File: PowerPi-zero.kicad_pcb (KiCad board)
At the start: 2 copper layers, 65 x 30 mm, 38 parts, among them J1 2444, J2 JST XH 01x02, J6 Raspberry_Pi_2_3, J8 JST XH 01x02, Q1 30V 4A 44mΩ, Q2 50nA 150V 200mW 200mA, Q3 30V 4A 44mΩ, U1 XL4015

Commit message: Final tweaks for producion
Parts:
- moved F1 1.08 mm to (101.5, 117.1)
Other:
- board text added: "V2.0"
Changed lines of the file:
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@@
     (pad_to_mask_clearance 0)
     (pcbplotparams
-      (layerselection 0x0001330_80000001)
+      (layerselection 0x00013f2_ffffffff)
       (disableapertmacros false)
       (usegerberextensions false)
@@
       (sketchpadsonfab false)
       (subtractmaskfromsilk false)
-      (outputformat 4)
+      (outputformat 1)
       (mirror false)
-      (drillshape 2)
+      (drillshape 0)
       (scaleselection 1)
       (outputdirectory "meta/")
@@
   )
   (footprint "Fuse:Fuse_Littelfuse-NANO2-451_453" (layer "F.Cu")
-    (at 101.5 116 90)
+    (at 101.5 117.085 90)
     (descr "Littelfuse NANO2 https://www.littelfuse.com/~/media/electronics/datasheets/fuses/littelfuse_fuse_451_453_datasheet.pdf.pdf")
     (tags "Fuse Nano2")
@@
     (property "abv.Footprint" "SMD-2_5.03x9.73x3.81")
     (attr smd)
-    (fp_text reference "F1" (at -5 0 90 unlocked) (layer "F.SilkS")
+    (fp_text reference "F1" (at 0 0 90 unlocked) (layer "F.SilkS")
       (effects (font (size 1 1) (thickness 0.15)))
     )
@@
       (effects (font (size 1 1) (thickness 0.15)))
     )
-    (fp_line (start -1.215 1.455) (end 1.215 1.455) (layer "F.SilkS") (width 0.12))
-    (fp_line (start -1.215 -1.455) (end 1.215 -1.455) (layer "F.SilkS") (width 0.12))
-    (fp_line (start -3.69 -1.83) (end 3.69 -1.83) (layer "F.CrtYd") (width 0.05))
-    (fp_line (start 3.69 -1.83) (end 3.69 1.83) (layer "F.CrtYd") (width 0.05))
-    (fp_line (start -3.69 1.83) (end -3.69 -1.83) (layer "F.CrtYd") (width 0.05))
-    (fp_line (start 3.69 1.83) (end -3.69 1.83) (layer "F.CrtYd") (width 0.05))
+    (fp_line (start -0.9 1.455) (end 0.9 1.455) (layer "F.SilkS") (width 0.12))
+    (fp_line (start -0.9 -1.455) (end 0.9 -1.455) (layer "F.SilkS") (width 0.12))
+    (fp_line (start 5.4 -2) (end 5.4 2) (layer "F.CrtYd") (width 0.05))
+    (fp_line (start -5.4 2) (end -5.4 -2) (layer "F.CrtYd") (width 0.05))
+    (fp_line (start -5.4 -2) (end 5.4 -2) (layer "F.CrtYd") (width 0.05))
+    (fp_line (start 5.4 2) (end -5.4 2) (layer "F.CrtYd") (width 0.05))
     (fp_line (start -3.05 -1.345) (end -3.05 1.345) (layer "F.Fab") (width 0.1))
     (fp_line (start -3.05 1.345) (end 3.05 1.345) (layer "F.Fab") (width 0.1))
     (fp_line (start -3.05 -1.345) (end 3.05 -1.345) (layer "F.Fab") (width 0.1))
     (fp_line (start 3.05 1.345) (end 3.05 -1.345) (layer "F.Fab") (width 0.1))
-    (pad "1" smd rect (at -2.455 0 90) (size 1.96 3.15) (layers "F.Cu" "F.Paste" "F.Mask")
+    (pad "1" smd rect (at -3.185 0 90) (size 4.24 3.81) (layers "F.Cu" "F.Paste" "F.Mask")
       (net 8 "Net-(F1-Pad1)") (pintype "passive") (zone_connect 2))
-    (pad "2" smd rect (at 2.455 0 90) (size 1.96 3.15) (layers "F.Cu" "F.Paste" "F.Mask")
+    (pad "2" smd rect (at 3.185 0 90) (size 4.24 3.81) (layers "F.Cu" "F.Paste" "F.Mask")
       (net 9 "Net-(F1-Pad2)") (pintype "passive") (zone_connect 2))
     (model "${KICAD6_3DMODEL_DIR}/Fuse.3dshapes/Fuse_Littelfuse-NANO2-451_453.wrl"
@@
     (property "abv.Footprint" "SMD-ECAP-10x10")
     (attr smd)
-    (fp_text reference "C1" (at 0 0) (layer "F.SilkS")
+    (fp_text reference "C1" (at 0.6 -0.5) (layer "F.SilkS")
       (effects (font (size 1 1) (thickness 0.15)))
     )
@@
     (fp_line (start 4.95 3.4) (end 4.95 -2.35) (layer "F.Fab") (width 0.1))
     (fp_line (start -2.45 3.4) (end 4.95 3.4) (layer "F.Fab") (width 0.1))
-    (pad "1" thru_hole roundrect (at 0 0 90) (size 1.7 2) (drill 1) (layers *.Cu *.Mask) (roundrect_rratio 0.147059)
+    (pad "1" thru_hole roundrect (at 0 0 90) (size 1.7 2) (drill 1) (layers *.Cu *.Mask) (roundrect_rratio 0.1470588235)
       (net 8 "Net-(F1-Pad1)") (pinfunction "Pin_1") (pintype "passive"))
     (pad "2" thru_hole oval (at 2.5 0 90) (size 1.7 2) (drill 1) (layers *.Cu *.Mask)
@@
     (effects (font (size 0.8 0.8) (thickness 0.14)))
   )
+  (gr_text "V2.0" (at 148 114.9 90) (layer "F.SilkS")
+    (effects (font (size 1 1) (thickness 0.15)))
+  )
   (gr_text "-" (at 133.65 94.25) (layer "F.SilkS")
     (effects (font (size 1 1) (thickness 0.153)))
@@
         (xy 112.2 106.6)
         (xy 112.2 101.4)
-        (xy 116.7 101.4)
-        (xy 117.8 100.3)
-        (xy 152.9 100.3)
+        (xy 116.2 101.4)
+        (xy 117.8 99.8)
+        (xy 152.9 99.8)
         (xy 153.5 100.9)
       )
@@
         (xy 102.5 109.5)
         (xy 104.5 111.5)
-        (xy 104.5 115)
-        (xy 99 115)
-        (xy 98 114)
+        (xy 104.5 116.4)
+        (xy 99 116.4)
+        (xy 98 115.6)
         (xy 98 106)
       )
@@
       (pts
         (xy 97.25 100.5)
-        (xy 97.25 114.25)
-        (xy 98.75 115.75)
-        (xy 104.5 115.75)
-        (xy 104.5 121)
-        (xy 94 121)
+        (xy 97.3 116)
+        (xy 98.75 117.35)
+        (xy 104.5 117.35)
+        (xy 104.5 123)
+        (xy 94 123)
         (xy 90 117)
         (xy 90 100.5)

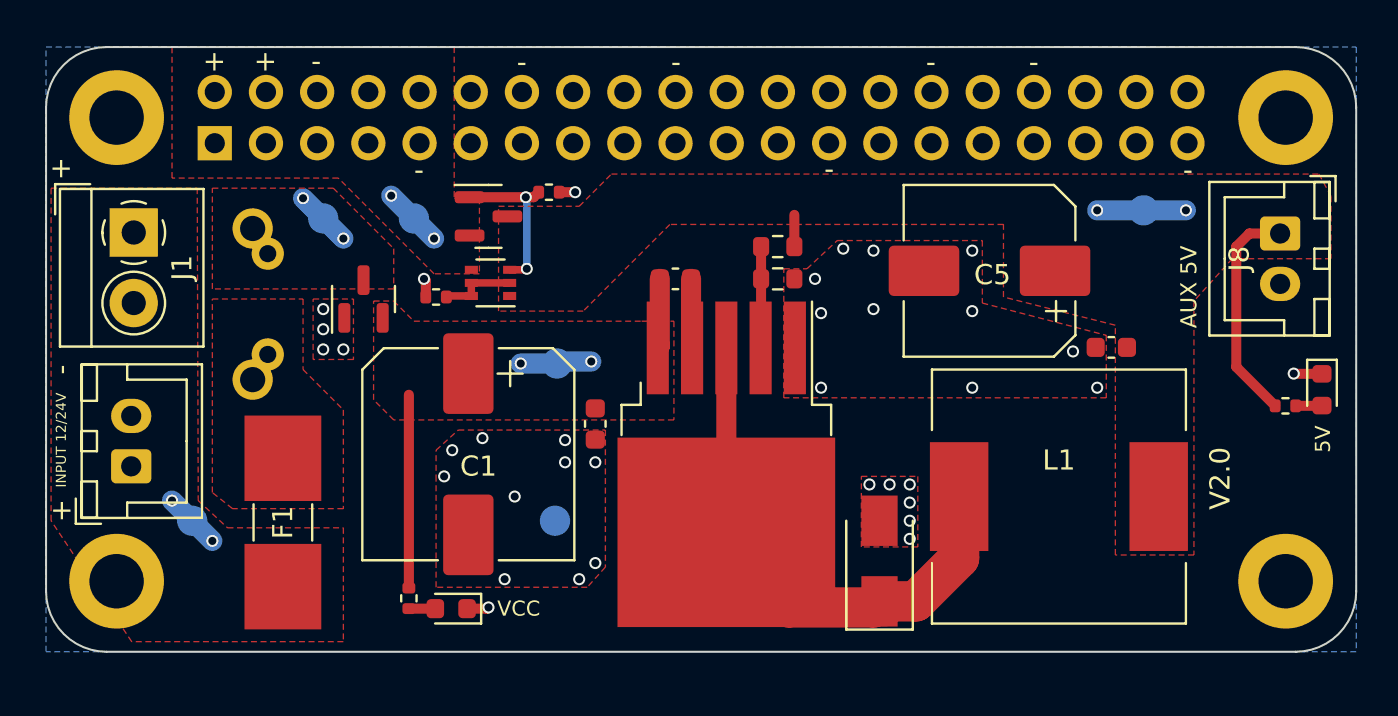
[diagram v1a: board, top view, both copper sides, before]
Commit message: Upgrade to TI part, matching ElectriPi.
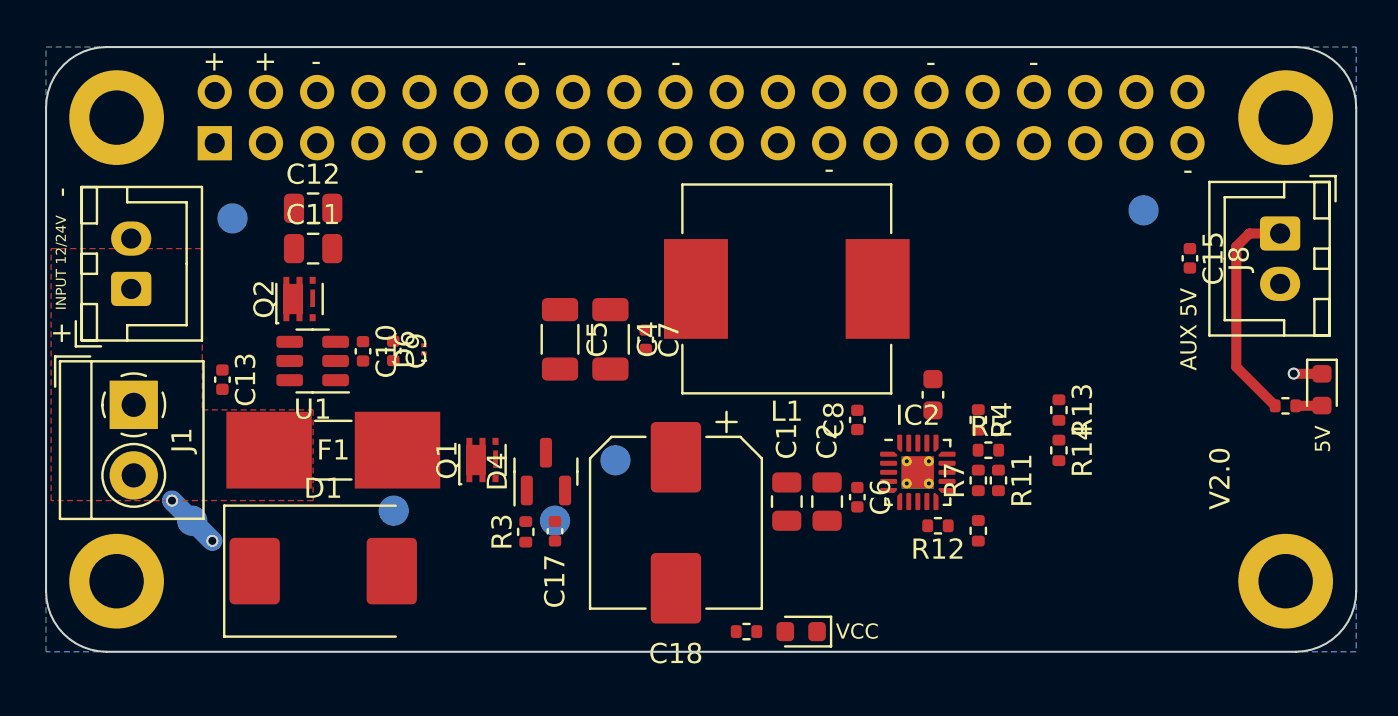
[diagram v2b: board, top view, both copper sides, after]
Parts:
- removed the G*** at (123.3, 117.0)
- removed Q3: 30V 4A 44mΩ, Package_TO_SOT_SMD:SOT-23
- removed R10: 10K, Resistor_SMD:R_0603_1608Metric
- removed R2: 47K, Resistor_SMD:R_0402_1005Metric
- removed R9: 3.3K, Resistor_SMD:R_0603_1608Metric
- removed TH1: ICL, Inrush_Limiter:5_OR_7pt5_PITCH_ICL
- added C10: 0.1uF, Capacitor_SMD:C_0402_1005Metric, F.Cu at (105.5, 108.6)
- added C11: 22 uF, Capacitor_SMD:C_0805_2012Metric, F.Cu at (103.0, 103.5)
- added C12: 22 uF, Capacitor_SMD:C_0805_2012Metric, F.Cu at (103.0, 101.5)
- added C13: 0.1uF, Capacitor_SMD:C_0402_1005Metric, F.Cu at (98.5, 110.0)
- added C15: 0.1uF, Capacitor_SMD:C_0402_1005Metric, F.Cu at (146.5, 104.0)
- added C17: 0.1uF, Capacitor_SMD:C_0402_1005Metric, F.Cu at (115.0, 117.5)
- added C18: 100uF, Capacitor_SMD:CP_Elec_8x10, F.Cu at (121.0, 117.1)
- added C6: 0.1uF, Capacitor_SMD:C_0402_1005Metric, F.Cu at (130.0, 115.8)
- added C7: 0.1uF, Capacitor_SMD:C_0402_1005Metric, F.Cu at (119.5, 108.0)
- added C8: 0.1uF, Capacitor_SMD:C_0402_1005Metric, F.Cu at (130.0, 112.0)
- added C9: 0.1uF, Capacitor_SMD:C_0402_1005Metric, F.Cu at (107.0, 108.6)
- added D1: XMC7K24CA, Diode_SMD:D_SMC, F.Cu at (103.5, 119.5)
- added D4: BZX84-C13, Package_TO_SOT_SMD:SOT-23, F.Cu at (114.5, 114.6)
- added IC2: TPS51397ARJER, Package_DFN_QFN:QFN-20-1EP_3x3mm_P0.45mm_EP1.6x1.6mm_ThermalVias, F.Cu at (133.0, 114.6)
- added R11: 33K, Resistor_SMD:R_0402_1005Metric, F.Cu at (137.0, 115.0)
- added R12: 110K, Resistor_SMD:R_0402_1005Metric, F.Cu at (134.0, 117.2)
- added R13: 110K, Resistor_SMD:R_0402_1005Metric, F.Cu at (140.0, 111.5)
- added R14: 15K, Resistor_SMD:R_0402_1005Metric, F.Cu at (140.0, 113.5)
- added R3: 110K, Resistor_SMD:R_0402_1005Metric, F.Cu at (113.5, 117.6)
- added R4: 180K, Resistor_SMD:R_0402_1005Metric, F.Cu at (136.0, 112.0)
- added R5: 33K, Resistor_SMD:R_0402_1005Metric, F.Cu at (136.5, 113.5)
- added R7: 110K, Resistor_SMD:R_0402_1005Metric, F.Cu at (136.0, 115.0)
- C1: value 220uF -> 22 uF; footprint Capacitor_SMD:CP_Elec_10x10 -> Capacitor_SMD:C_0805_2012Metric
- C2: value 1 uF -> 22 uF; footprint Capacitor_SMD:C_0603_1608Metric -> Capacitor_SMD:C_0805_2012Metric
- C4: value 1 uF -> 100uF; footprint Capacitor_SMD:C_0603_1608Metric -> Capacitor_SMD:C_1206_3216Metric
- C5: value 1000uF -> 100uF; footprint Capacitor_SMD:CP_Elec_8x10 -> Capacitor_SMD:C_1206_3216Metric
- D6: value SS54 -> PESD5V0C1BSFYL; footprint Diode_SMD:D_SMA -> Diode_SMD:Nexperia_DSN0603-2_0.6x0.3mm_P0.4mm
- L1: value 47 uH -> 1.8 uH; footprint Inductor_SMD:L_12x12mm_H6mm -> Inductor_SMD:L_Vishay_IHLP-4040
- Q1: value 30V 4A 44mΩ -> SiA471DJ; footprint Package_TO_SOT_SMD:SOT-23 -> Package_TO_SOT_SMD:Vishay_PowerPAK_SC70-6L_Single
- Q2: value 50nA 150V 200mW 200mA -> SiA430DJT; footprint Package_TO_SOT_SMD:SOT-363_SC-70-6 -> Package_TO_SOT_SMD:Vishay_PowerPAK_SC70-6L_Single
- R1: value 10K -> 33K
- R6: value 1kR -> 1K
- R8: value 10kR -> 10K
- U1: value XL4015 -> LM74700; footprint Package_TO_SOT_SMD:TO-263-5_TabPin3 -> Package_TO_SOT_SMD:SOT-23-6
- moved R1 29.3 mm to (136.0, 117.5), turned to -90 degrees
- moved D6 24.9 mm to (108.5, 108.5)
- moved C4 24.9 mm to (117.8, 108.0), turned to -90 degrees
- moved C5 21.6 mm to (115.2, 108.0), turned to -90 degrees
- moved U1 21.2 mm to (103.0, 109.1), turned to 180 degrees
- moved D5 17.4 mm to (127.2, 122.5)
- moved L1 17.0 mm to (126.5, 105.5), turned to 180 degrees
- moved R8 16.8 mm to (124.5, 122.5), turned to 180 degrees
- moved C1 16.0 mm to (126.5, 116.0)
- moved TP3 14.9 mm to (107.0, 116.5)
- moved C3 14.0 mm to (133.8, 110.8), turned to 90 degrees
- moved C2 12.1 mm to (128.5, 116.0)
- moved Q1 9.93 mm to (111.4, 114.0)
- moved Q2 9.51 mm to (102.3, 106.0), turned to 90 degrees
- moved TP5 9.00 mm to (99.0, 102.0)
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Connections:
- C1 pad 1: VCC -> Vin
- C2 pad 1: VCC -> Vin
- C3 pad 1: Net-(C3-Pad1) -> VCC
- C3 pad 2: VCC -> GND
- D6 pad 1: Net-(D6-Pad1) -> GND
- D6 pad 2: GND -> +5V
- F1 pad 2: Net-(F1-Pad2) -> Net-(D1-A2)
- L1 pad 1: Net-(D6-Pad1) -> SW
- Q1 pad 1: GND -> Net-(D1-A2)
- Q1 pad 3: Net-(Q1-Pad3) -> Net-(D4-A)
- Q2 pad 1: +5V -> 5V_PI
- Q2 pad 3: Net-(Q2-Pad3) -> Net-(Q2-G)
- Q2 pad 4: 5V_PI -> +5V
- R1 pad 1: Net-(Q2-Pad2) -> Net-(R1-Pad1)
- R1 pad 2: GND -> Vin
- R8 pad 2: VCC -> Vin
- TP3 pad 1: Net-(Q1-Pad3) -> Net-(D1-A2)
- TP4 pad 1: VCC -> Vin
- U1 pad 1: GND -> Net-(U1-VCAP)
- U1 pad 2: Net-(R10-Pad1) -> GND
- U1 pad 3: Net-(D6-Pad1) -> +5V
- U1 pad 4: Net-(C3-Pad1) -> 5V_PI
- U1 pad 5: VCC -> Net-(Q2-G)
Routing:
- net Net-(D6-Pad1): track 26.4 -> 0.00 mm
- net VCC: track 16.5 -> 0.00 mm, vias 2 -> 0
- net Net-(Q2-Pad3): track 7.97 -> 0.00 mm, vias 2 -> 0
- net +5V: track 17.1 -> 11.1 mm, vias 2 -> 0
- net Net-(R10-Pad1): track 5.00 -> 0.00 mm
- net Net-(Q2-Pad2): track 3.74 -> 0.00 mm
- net Net-(C3-Pad1): track 3.38 -> 0.00 mm
- net 5V_PI: track 3.01 -> 0.00 mm, vias 2 -> 0
- net Net-(Q1-Pad3): track 2.83 -> 0.00 mm, vias 2 -> 0
- net GND: track 4.22 -> 1.41 mm, vias 35 -> 1
- net Net-(D5-A): track 1.31 -> 0.00 mm
- removed copper zone on F.Cu, net +5V
- removed copper zone on F.Cu, net 5V_PI
- removed copper zone on F.Cu, net GND
- removed copper zone on F.Cu, net Net-(F1-Pad2)
- removed copper zone on F.Cu, net Net-(Q1-Pad3)
- removed copper zone on F.Cu, net VCC
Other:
- board text removed: "Manufactured by LDO Motors"

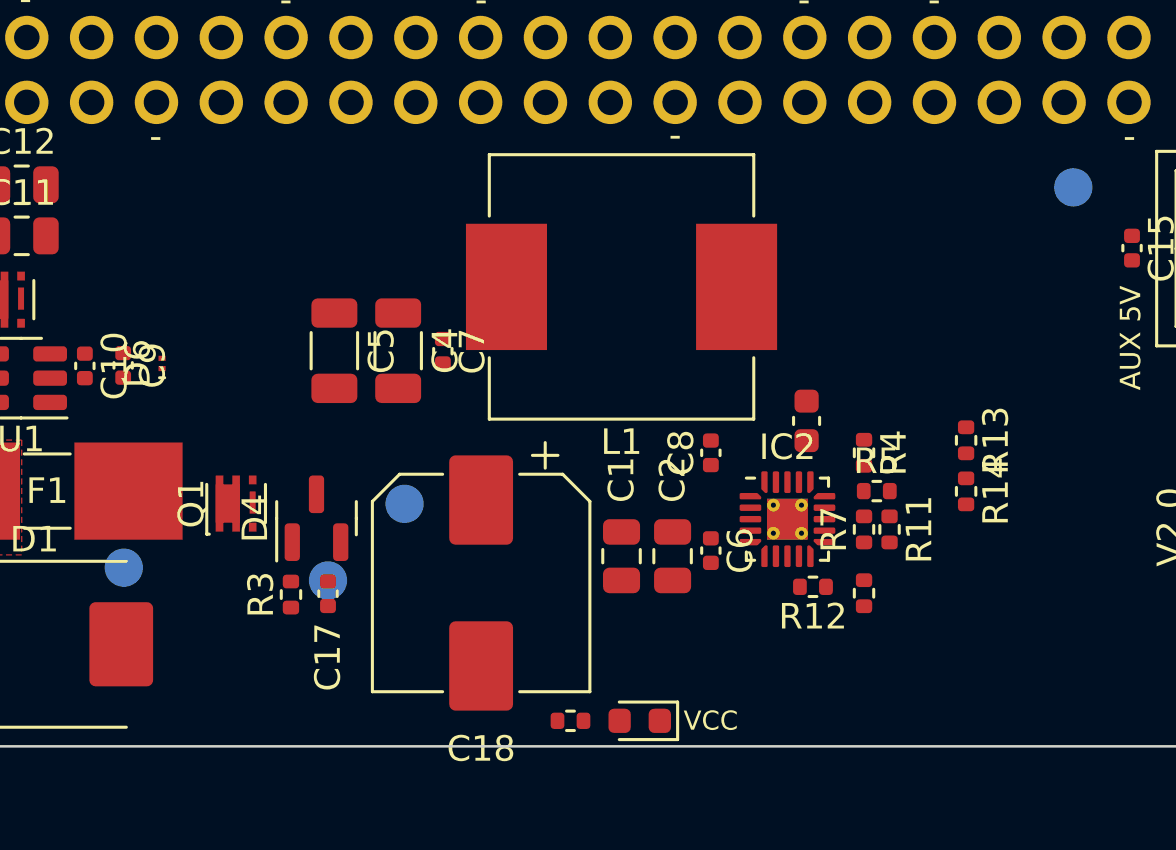
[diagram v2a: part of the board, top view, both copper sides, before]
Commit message: alter component position
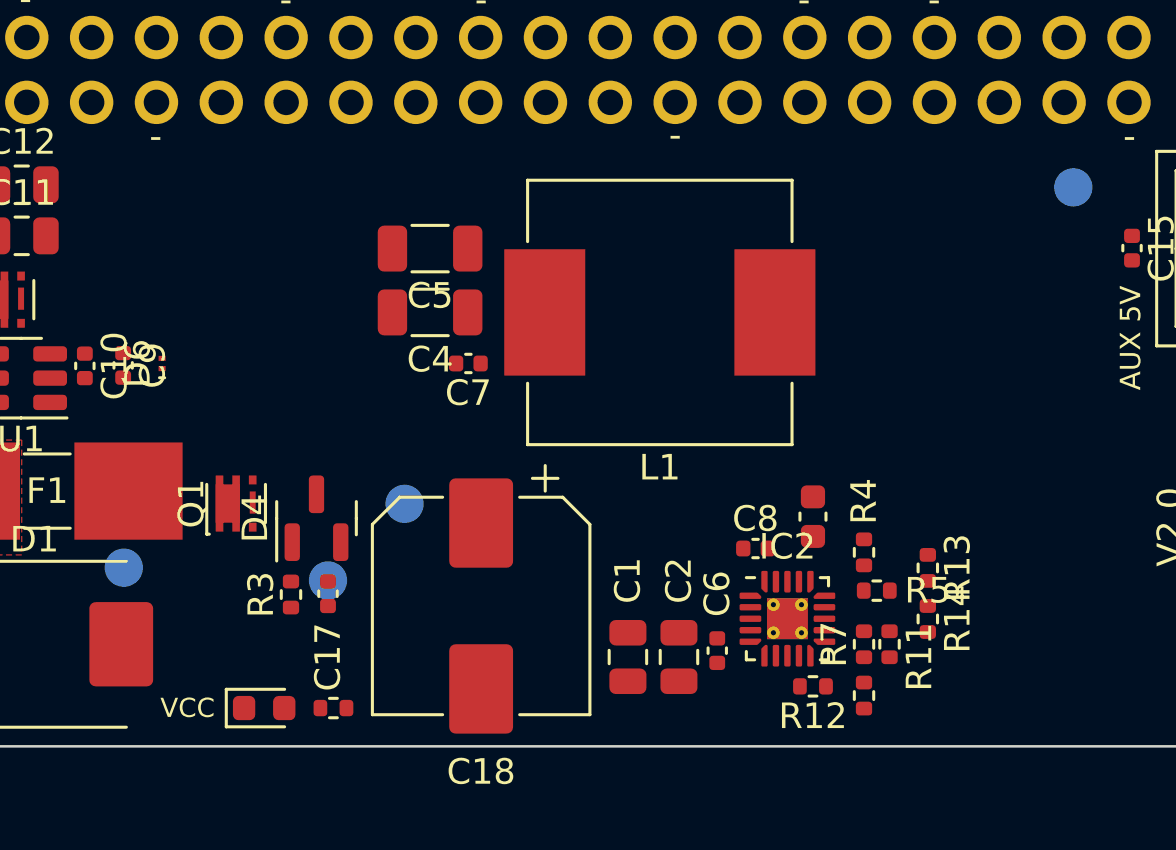
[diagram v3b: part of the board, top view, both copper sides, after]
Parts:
- moved D5 14.7 mm to (112.5, 122.0), turned to 0 degrees
- moved R8 9.30 mm to (115.2, 122.0), turned to 0 degrees
- moved C5 5.48 mm to (119.0, 104.0), turned to 180 degrees
- moved R13 5.22 mm to (138.5, 116.5)
- moved R14 5.22 mm to (138.5, 118.5)
- moved R11 4.50 mm to (137.0, 119.5)
- moved R7 4.50 mm to (136.0, 119.5)
- moved C8 4.14 mm to (131.8, 115.8), turned to 0 degrees
- moved R1 4.01 mm to (136.0, 121.5)
- moved C1 3.96 mm to (126.8, 120.0)
- moved C2 3.96 mm to (128.8, 120.0)
- moved C6 3.93 mm to (130.2, 119.8)
- moved IC2 3.90 mm to (133.0, 118.5)
- moved R12 3.90 mm to (134.0, 121.2)
- moved R4 3.90 mm to (136.0, 115.9)
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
